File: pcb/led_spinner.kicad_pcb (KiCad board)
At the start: 2 copper layers, 0 parts

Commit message: Add board outline to pcb. Add modules with rough (relative) positioning.
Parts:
- added BT1: BATTERY_CR2032, battery-cr2032-retainer-keystone-3003:CR2032_HOLDER_KEYSTONE_3003, B.Cu at (194.3, 106.7)
- added C1: C, w_smd_cap:c_0805, F.Cu at (195.6, 113.0)
- added C2: C, w_smd_cap:c_0805, F.Cu at (191.8, 113.0)
- added C3: C, w_smd_cap:c_0805, F.Cu at (201.9, 109.2)
- added CON1: AVR-ISP-6, w_pin_strip:pin_socket_3x2, B.Cu at (194.3, 91.4)
- added J1: SERIAL, w_pin_strip:pin_socket_3, F.Cu at (179.1, 111.8)
- added J2: SPARE, w_pin_strip:pin_socket_2, F.Cu at (184.2, 120.7)
- added J3: TILT, w_pin_strip:pin_socket_2, F.Cu at (177.8, 116.8)
- added LD1: LED, w_smd_leds:Led_0805, F.Cu at (152.4, 95.2)
- added LD10: LED, w_smd_leds:Led_0805, F.Cu at (160.0, 123.2)
- added LD11: LED, w_smd_leds:Led_0805, F.Cu at (165.1, 92.7)
- added LD12: LED, w_smd_leds:Led_0805, F.Cu at (165.1, 104.1)
- added LD13: LED, w_smd_leds:Led_0805, F.Cu at (165.1, 108.0)
- added LD14: LED, w_smd_leds:Led_0805, F.Cu at (165.1, 120.7)
- added LD15: LED, w_smd_leds:Led_0805, F.Cu at (168.9, 96.5)
- added LD16: LED, w_smd_leds:Led_0805, F.Cu at (170.2, 111.8)
- added LD2: LED, w_smd_leds:Led_0805, F.Cu at (148.6, 114.3)
- added LD3: LED, w_smd_leds:Led_0805, F.Cu at (156.2, 92.7)
- added LD4: LED, w_smd_leds:Led_0805, F.Cu at (156.2, 99.1)
- added LD5: LED, w_smd_leds:Led_0805, F.Cu at (154.9, 108.0)
- added LD6: LED, w_smd_leds:Led_0805, F.Cu at (154.9, 116.8)
- added LD7: LED, w_smd_leds:Led_0805, F.Cu at (160.0, 90.2)
- added LD8: LED, w_smd_leds:Led_0805, F.Cu at (160.0, 105.4)
- added LD9: LED, w_smd_leds:Led_0805, F.Cu at (160.0, 108.0)
- added R1: R, w_smd_resistors:r_0805, F.Cu at (188.0, 106.7)
- added R10: R, w_smd_resistors:r_0805, F.Cu at (160.0, 110.5)
- added R11: R, w_smd_resistors:r_0805, F.Cu at (160.0, 120.7)
- added R12: R, w_smd_resistors:r_0805, F.Cu at (165.1, 95.2)
- added R13: R, w_smd_resistors:r_0805, F.Cu at (165.1, 101.6)
- added R14: R, w_smd_resistors:r_0805, F.Cu at (165.1, 110.5)
- added R15: R, w_smd_resistors:r_0805, F.Cu at (165.1, 118.1)
- added R16: R, w_smd_resistors:r_0805, F.Cu at (168.9, 99.1)
- added R17: R, w_smd_resistors:r_0805, F.Cu at (170.2, 114.3)
- added R2: R, w_smd_resistors:r_0805, F.Cu at (152.4, 97.8)
- added R3: R, w_smd_resistors:r_0805, F.Cu at (152.4, 114.3)
- added R4: R, w_smd_resistors:r_0805, F.Cu at (156.2, 95.2)
- added R5: R, w_smd_resistors:r_0805, F.Cu at (156.2, 101.6)
- added R6: R, w_smd_resistors:r_0805, F.Cu at (154.9, 110.5)
- added R7: R, w_smd_resistors:r_0805, F.Cu at (154.9, 119.4)
- added R8: R, w_smd_resistors:r_0805, F.Cu at (160.0, 92.7)
- added R9: R, w_smd_resistors:r_0805, F.Cu at (160.0, 102.9)
- added SW1: SW_PUSH_ALT, OMRON-PUSH-BUTTON-B3SN-3112P:OMRON-PUSH-BUTTON-B3SN-3112P, F.Cu at (194.3, 121.9)
- added U1: ATMEGA48_88_168_328P-32SMD, w_smd_lqfp:lqfp32, F.Cu at (194.3, 106.7)
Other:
- board outline added: 48.3 x 48.3 mm

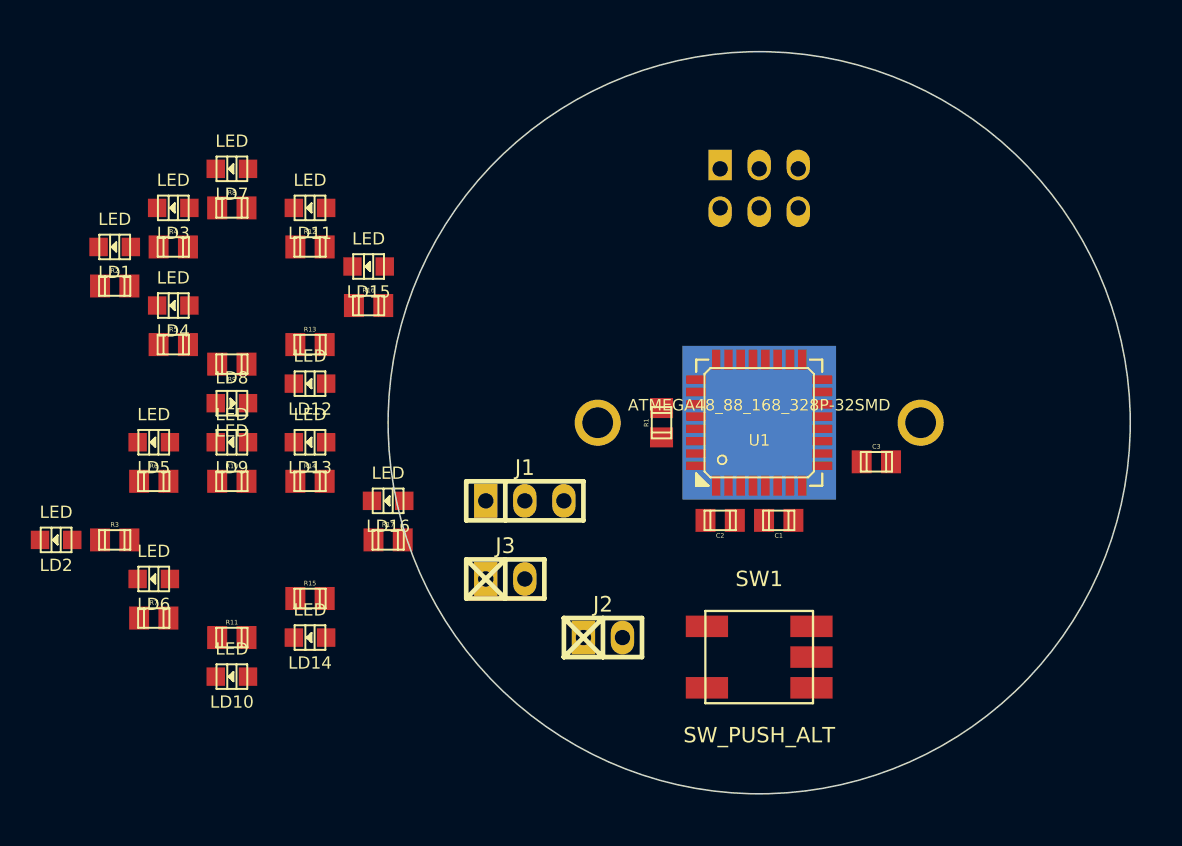
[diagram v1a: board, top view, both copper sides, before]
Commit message: Move four N,E,S,W front LEDs into correct place (based on current board size).
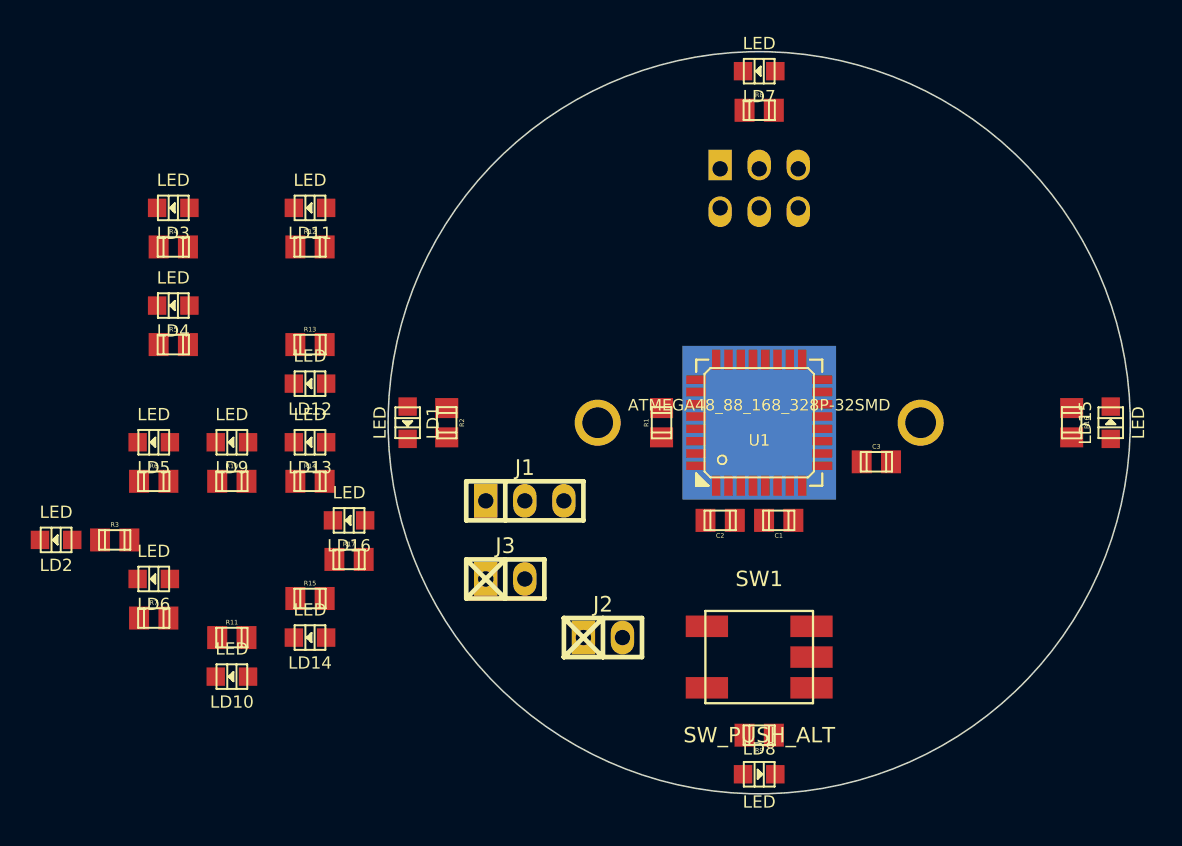
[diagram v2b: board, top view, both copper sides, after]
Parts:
- moved LD15 49.3 mm to (217.2, 106.7), turned to 90 degrees
- moved R16 46.4 mm to (214.6, 106.7), turned to 270 degrees
- moved LD8 41.9 mm to (194.3, 129.5)
- moved R9 41.9 mm to (194.3, 127.0)
- moved LD7 34.9 mm to (194.3, 83.8)
- moved R8 34.9 mm to (194.3, 86.4)
- moved R2 23.3 mm to (174.0, 106.7), turned to 270 degrees
- moved LD1 22.2 mm to (171.4, 106.7), turned to 270 degrees
- moved LD16 2.84 mm to (167.6, 113.0)
- moved R17 2.84 mm to (167.6, 115.6)

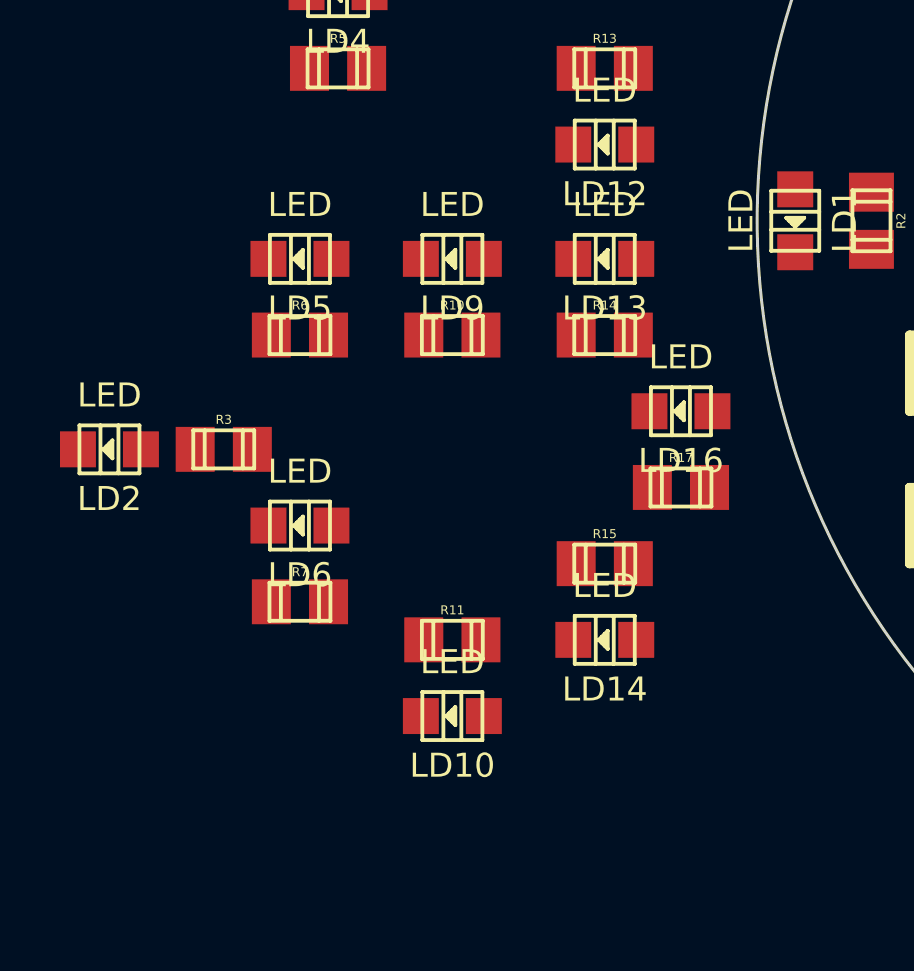
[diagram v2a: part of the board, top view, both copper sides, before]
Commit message: Move all back side LEDs to the back of the board.
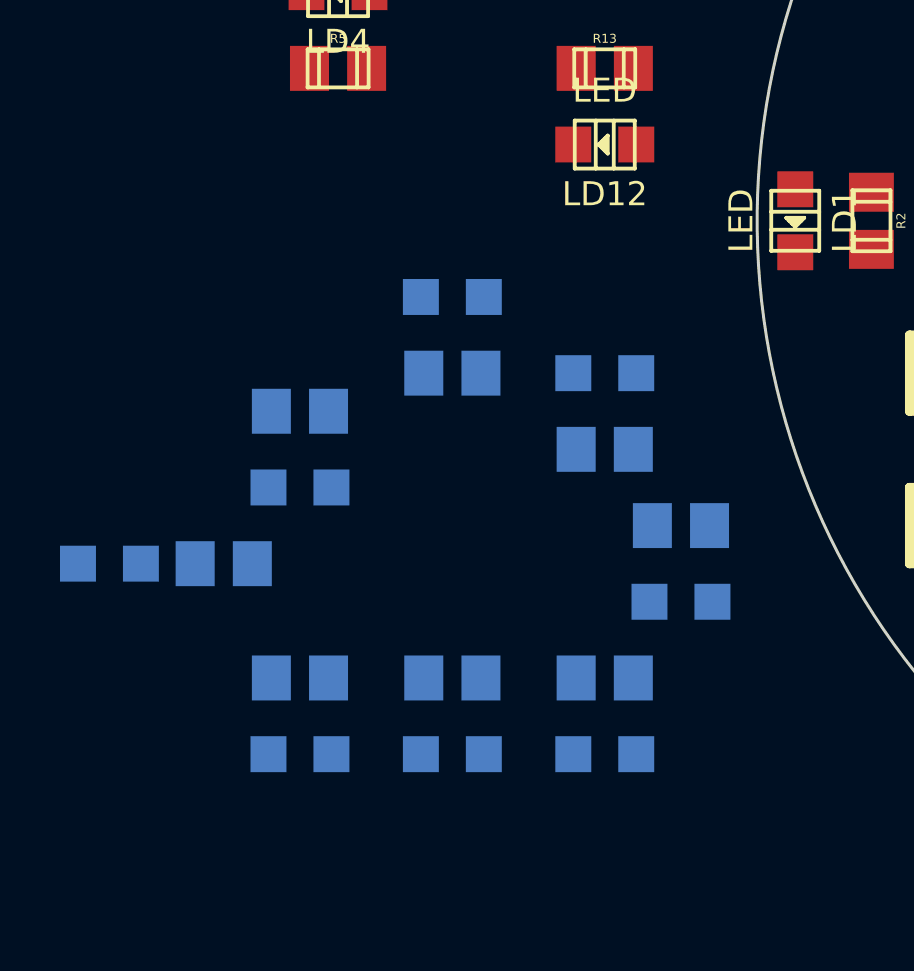
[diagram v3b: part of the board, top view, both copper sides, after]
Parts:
- LD10, LD13, LD14, LD16, LD2, LD5, LD6, LD9, R10, R11, R14, R15, R17, R3, R6, R7: moved to B.Cu
- moved LD13 16.5 mm to (165.1, 124.5)
- moved LD5 16.5 mm to (154.9, 124.5)
- moved LD9 16.5 mm to (160.0, 124.5)
- moved LD10 14.0 mm to (160.0, 109.2)
- moved R10 11.4 mm to (160.0, 121.9)
- moved R14 11.4 mm to (165.1, 121.9)
- moved R6 11.4 mm to (154.9, 121.9)
- moved LD14 8.89 mm to (165.1, 111.8)
- moved R11 8.89 mm to (160.0, 111.8)
- moved LD16 6.35 mm to (167.6, 119.4)
- moved R7 6.35 mm to (154.9, 113.0)
- moved LD2 3.81 mm to (148.6, 118.1)
- moved R15 3.81 mm to (165.1, 114.3)
- moved R3 3.81 mm to (152.4, 118.1)
- moved LD6 1.27 mm to (154.9, 115.6)
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
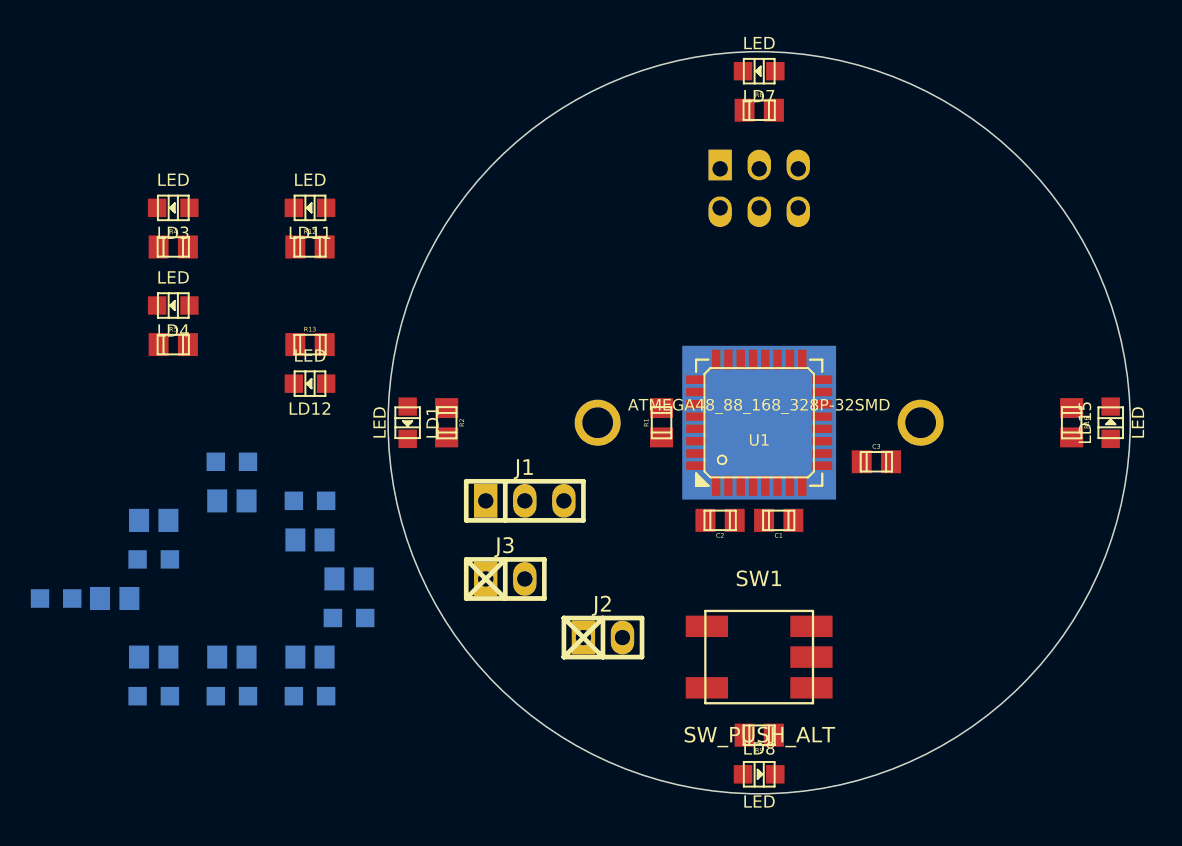
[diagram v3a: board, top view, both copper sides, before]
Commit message: Move front NE,SE,SW,NW LEDs into position. The positions aren't entirely perfect due to interaction between the 45 degree angle and the forced snap to grid.
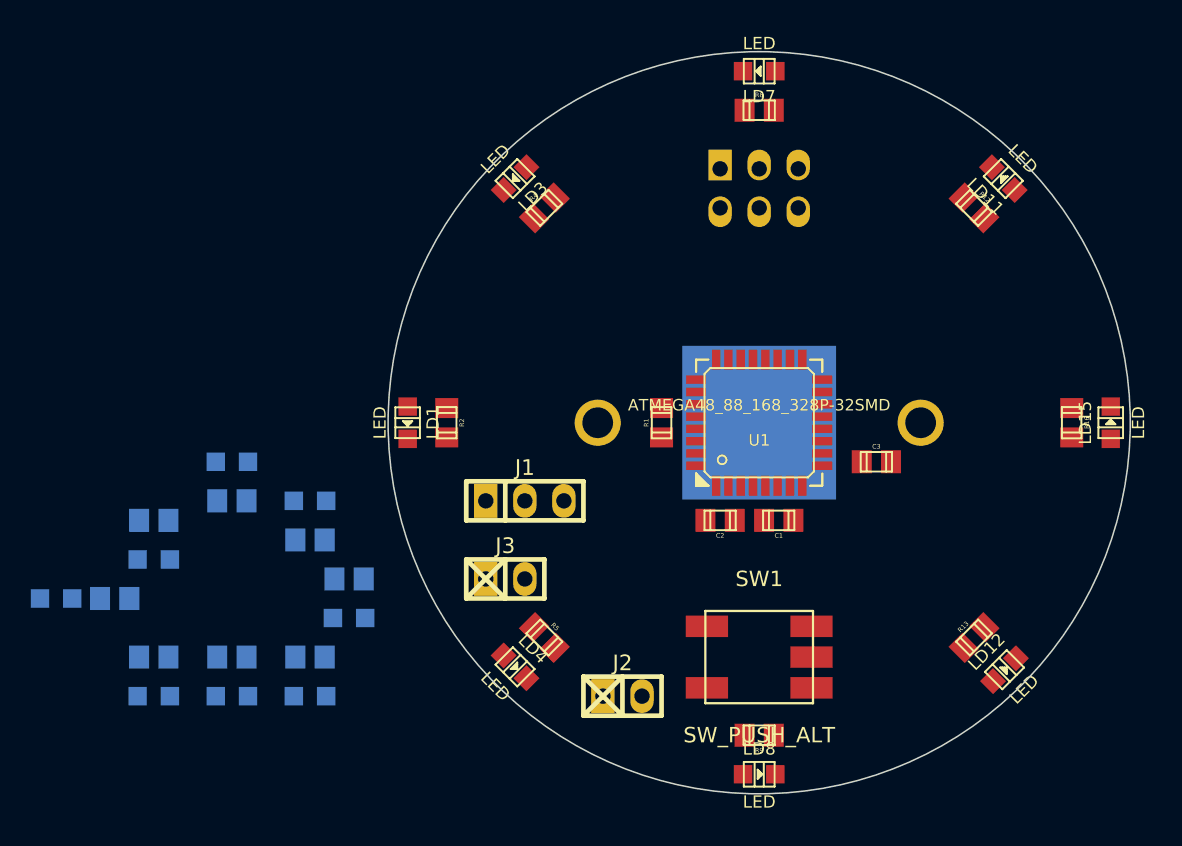
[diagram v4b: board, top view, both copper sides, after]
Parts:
- moved LD12 48.8 mm to (210.3, 122.7), turned to 45 degrees
- moved R13 47.2 mm to (208.3, 120.7), turned to 45 degrees
- moved LD11 45.1 mm to (210.2, 90.8), turned to 135 degrees
- moved R12 43.3 mm to (208.3, 92.7), turned to 315 degrees
- moved LD4 32.3 mm to (178.4, 122.6), turned to 315 degrees
- moved R5 30.7 mm to (180.3, 120.7), turned to 315 degrees
- moved R4 24.3 mm to (180.3, 92.7), turned to 45 degrees
- moved LD3 22.3 mm to (178.4, 90.8), turned to 225 degrees
- moved J2 4.02 mm to (185.4, 124.5)
